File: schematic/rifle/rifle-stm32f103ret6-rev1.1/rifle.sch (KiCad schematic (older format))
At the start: 47 parts, among them K1 Magazine, K3 IR_LASER, P10 RFID-RC522-MODULE, P11 NRF24L01, P12 VibroEng, P13 IR_LED, P14 Power_in, P3 Reset, P6 SWD_IO, P7 SWD_CLK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

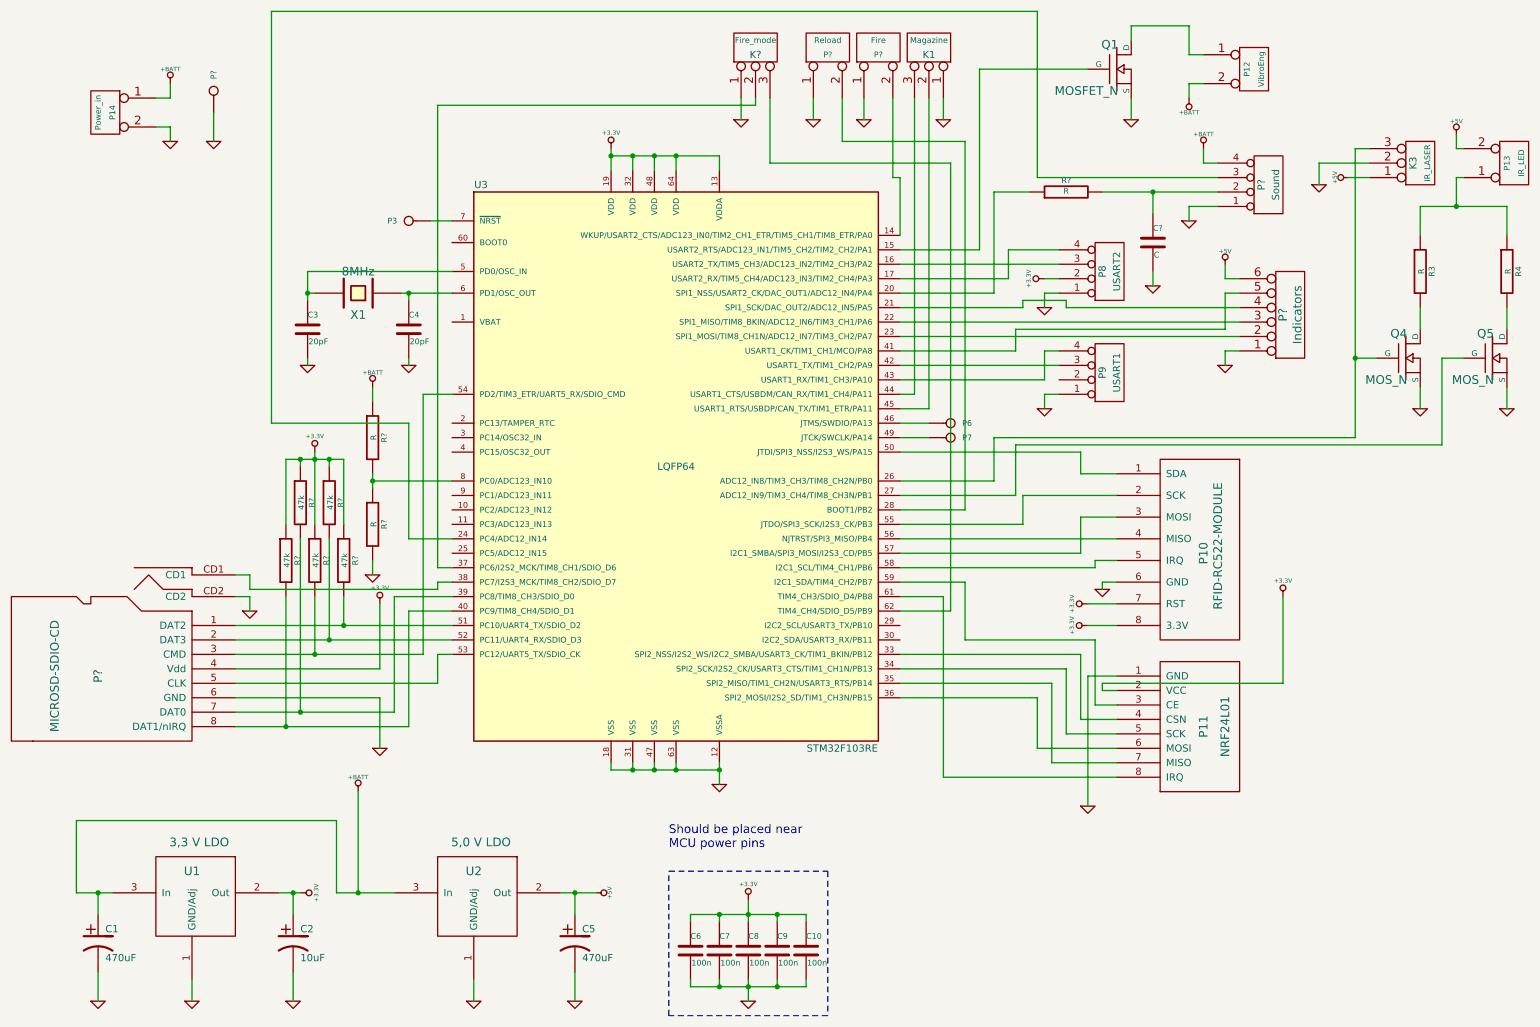
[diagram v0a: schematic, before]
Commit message: Rifle r1.1 pcb beginned
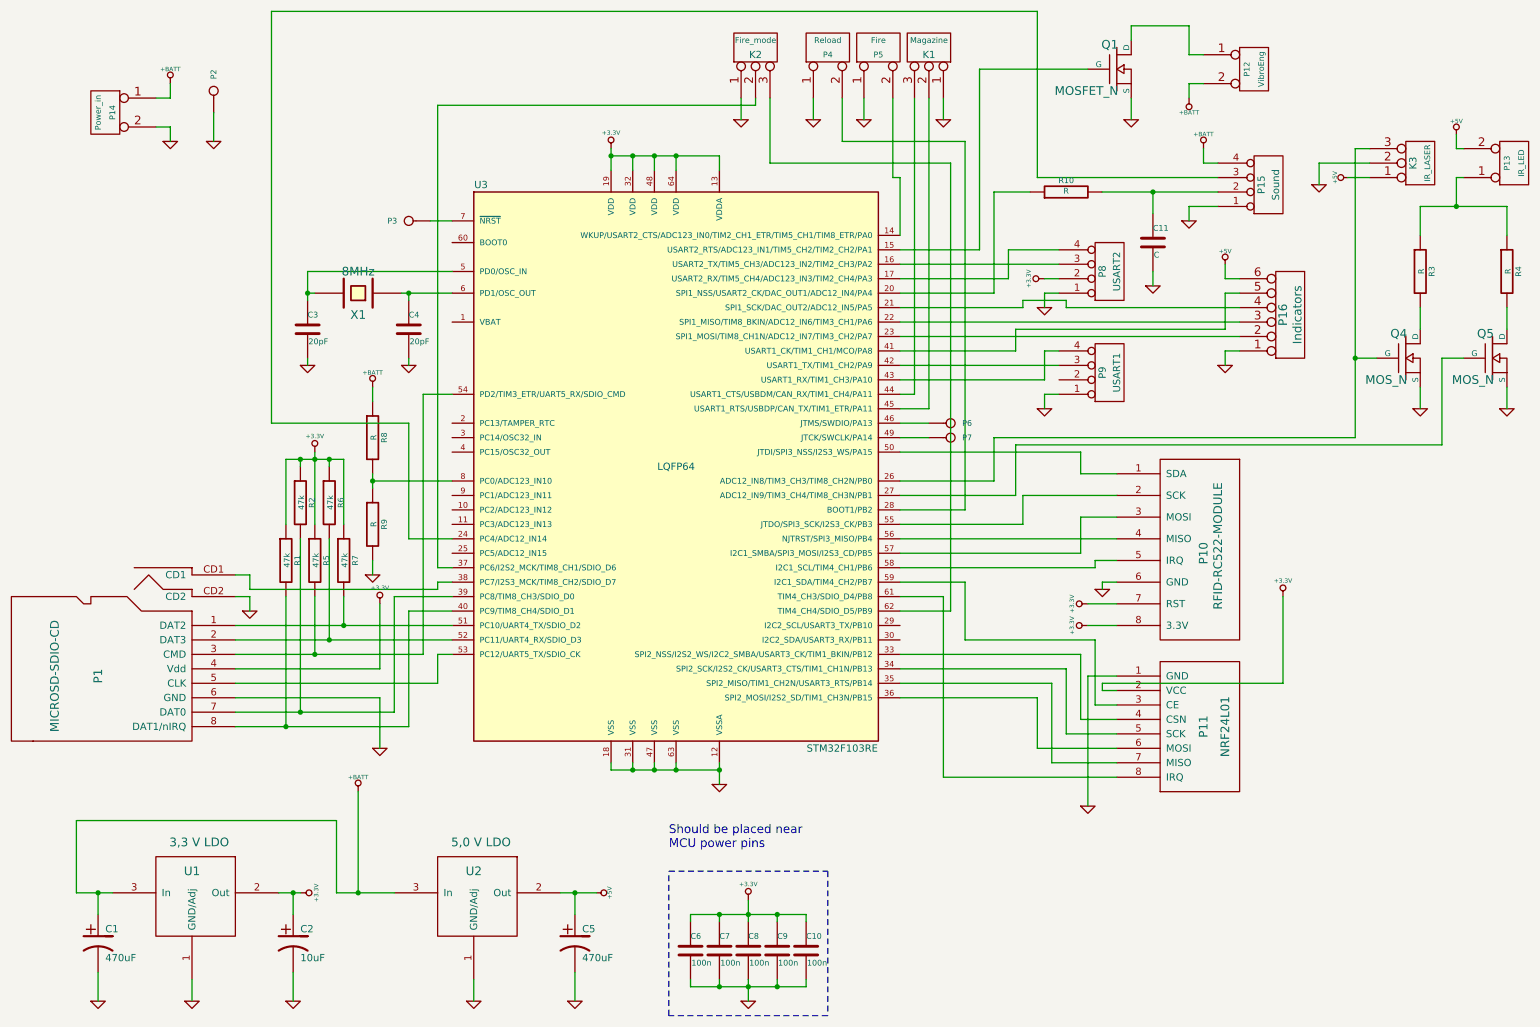
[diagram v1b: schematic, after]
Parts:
- gave numbers to parts that had none: 16

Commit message: WIP rifle 1.1 pcb
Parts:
- added P17: FireFlash, ~, symbol CONN_2
- added Q2: MOS_N, ~, symbol MOS_N
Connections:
- net +3.3V: now also P17.2 (PM)
- net GND: now also Q2.S
- net at U3.30 (I2C2_SDA/USART3_RX/PB11): now also Q2.G
- new net: P17.1 (P1), Q2.D
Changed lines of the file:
@@
 Wire Wire Line
 	7600 1800 8850 1800
+$Comp
+L CONN_2 P17
+U 1 1 54E6464E
+P 7950 6500
+F 0 "P17" V 7900 6500 40  0000 C CNN
+F 1 "FireFlash" V 8000 6500 40  0000 C CNN
+F 2 "~" H 7950 6500 60  0000 C CNN
+F 3 "~" H 7950 6500 60  0000 C CNN
+	1    7950 6500
+	1    0    0    -1
+$EndComp
+$Comp
+L GND #PWR048
+U 1 1 54E6465D
+P 7150 6850
+F 0 "#PWR048" H 7150 6850 30  0001 C CNN
+F 1 "GND" H 7150 6780 30  0001 C CNN
+F 2 "" H 7150 6850 60  0000 C CNN
+F 3 "" H 7150 6850 60  0000 C CNN
+	1    7150 6850
+	1    0    0    -1
+$EndComp
+$Comp
+L MOS_N Q2
+U 1 1 54E64676
+P 7050 6500
+F 0 "Q2" H 7060 6670 60  0000 R CNN
+F 1 "MOS_N" H 7060 6350 60  0000 R CNN
+F 2 "~" H 7050 6500 60  0000 C CNN
+F 3 "~" H 7050 6500 60  0000 C CNN
+	1    7050 6500
+	1    0    0    -1
+$EndComp
+Wire Wire Line
+	7150 6300 7150 6200
+Wire Wire Line
+	7150 6200 7500 6200
+Wire Wire Line
+	7500 6200 7500 6400
+Wire Wire Line
+	7500 6400 7600 6400
+Wire Wire Line
+	7150 6700 7150 6850
+Wire Wire Line
+	6650 5000 6750 5000
+Wire Wire Line
+	6750 5000 6750 6500
+Wire Wire Line
+	6750 6500 6850 6500
+$Comp
+L +3.3V #PWR?
+U 1 1 54E65921
+P 7500 6600
+F 0 "#PWR?" H 7500 6560 30  0001 C CNN
+F 1 "+3.3V" H 7500 6710 30  0000 C CNN
+F 2 "" H 7500 6600 60  0000 C CNN
+F 3 "" H 7500 6600 60  0000 C CNN
+	1    7500 6600
+	0    -1   -1   0
+$EndComp
+Wire Wire Line
+	7500 6600 7600 6600
 $EndSCHEMATC

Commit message: Rifle pcb seems done
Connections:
- net +3.3V: no longer P17.2 (PM)
- net +BATT: now also P17.2 (PM)
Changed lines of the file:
@@
 Sheet 1 1
 Title ""
-Date "19 feb 2015"
+Date "20 feb 2015"
 Rev ""
 Comp ""
@@
 Wire Wire Line
 	6750 6500 6850 6500
-$Comp
-L +3.3V #PWR?
-U 1 1 54E65921
-P 7500 6600
-F 0 "#PWR?" H 7500 6560 30  0001 C CNN
-F 1 "+3.3V" H 7500 6710 30  0000 C CNN
-F 2 "" H 7500 6600 60  0000 C CNN
-F 3 "" H 7500 6600 60  0000 C CNN
-	1    7500 6600
+Wire Wire Line
+	7450 6600 7600 6600
+$Comp
+L +BATT #PWR?
+U 1 1 54E709C2
+P 7450 6600
+F 0 "#PWR?" H 7450 6550 20  0001 C CNN
+F 1 "+BATT" H 7450 6700 30  0000 C CNN
+F 2 "" H 7450 6600 60  0000 C CNN
+F 3 "" H 7450 6600 60  0000 C CNN
+	1    7450 6600
 	0    -1   -1   0
 $EndComp
-Wire Wire Line
-	7500 6600 7600 6600
 $EndSCHEMATC
